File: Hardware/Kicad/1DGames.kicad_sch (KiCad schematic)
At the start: 0 parts

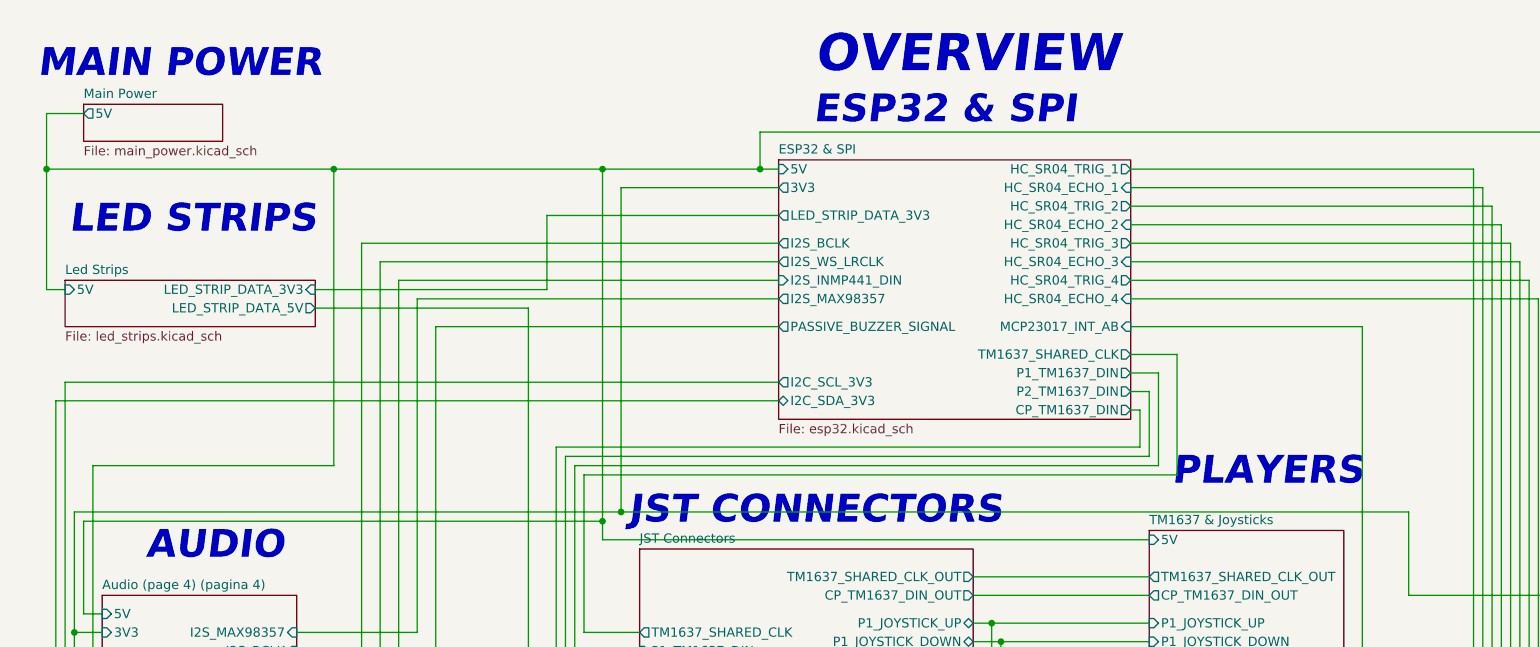
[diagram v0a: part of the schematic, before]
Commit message: New Fraxis PCB layout
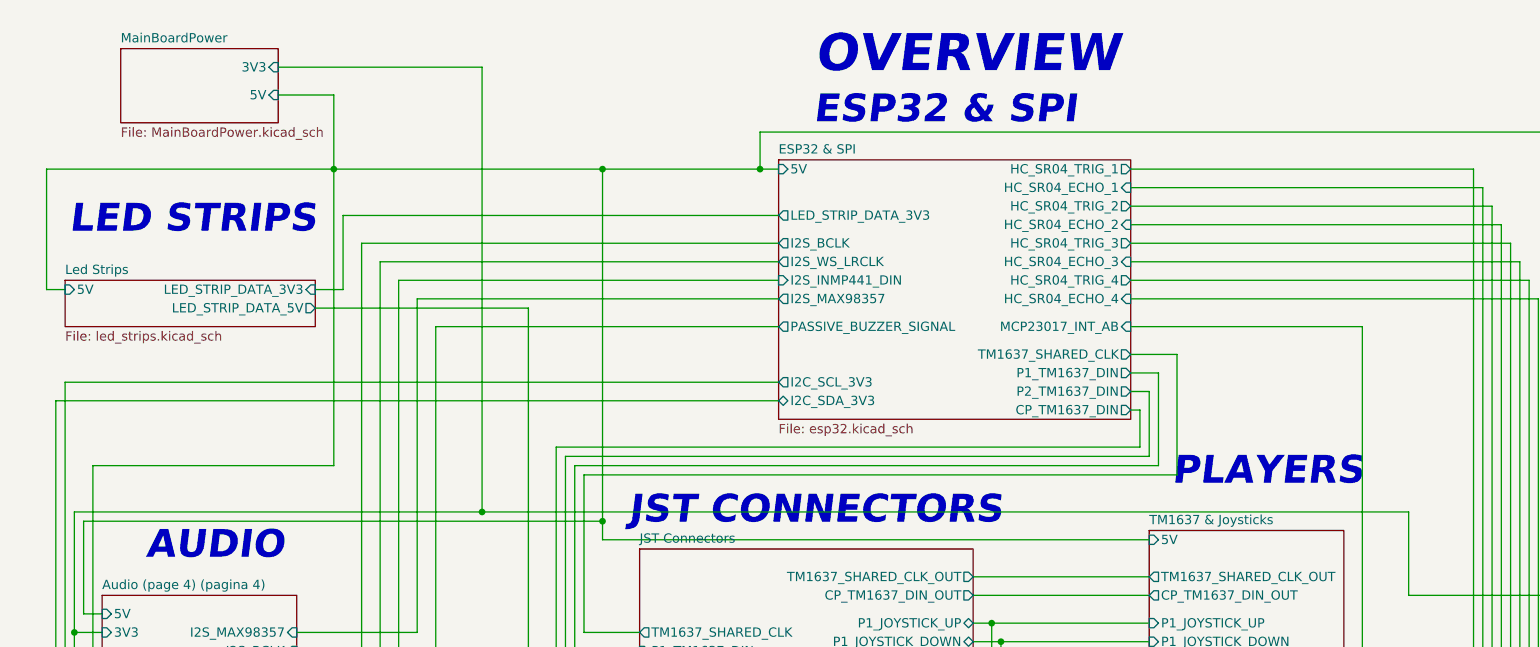
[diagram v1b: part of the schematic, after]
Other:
- removed sheet Main Power
- added sheet MainBoardPower (MainBoardPower.kicad_sch)
- sheet ESP32 & SPI ports: added none; removed 3V3
- note removed: "MAIN POWER"
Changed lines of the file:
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@@
 		)
 	)
-	(text "MAIN POWER"
-		(exclude_from_sim no)
-		(at 34.798 20.828 0)
-		(effects
-			(font
-				(size 3.81 3.81)
-				(thickness 0.4013)
-				(bold yes)
-				(italic yes)
-			)
-			(justify bottom)
-		)
-	)
 	(text "ESP32 & SPI"
 		(exclude_from_sim no)
@@
 	)
 	(junction
-		(at 95.25 80.01)
-		(diameter 0)
-		(color 0 0 0 0)
-	)
-	(junction
 		(at 212.09 113.03)
 		(diameter 0)
@@
 	)
 	(junction
-		(at 16.51 33.02)
+		(at 76.2 80.01)
 		(diameter 0)
 		(color 0 0 0 0)
@@
 	(wire
 		(pts
-			(xy 16.51 33.02) (xy 16.51 25.4)
-		)
-		(stroke
-			(width 0)
-			(type default)
-		)
-	)
-	(wire
-		(pts
 			(xy 87.63 135.89) (xy 87.63 113.03)
 		)
@@
 	(wire
 		(pts
+			(xy 48.26 22.86) (xy 55.88 22.86)
+		)
+		(stroke
+			(width 0)
+			(type default)
+		)
+	)
+	(wire
+		(pts
 			(xy 156.21 119.38) (xy 167.64 119.38)
 		)
@@
 	(wire
 		(pts
-			(xy 116.84 39.37) (xy 85.09 39.37)
+			(xy 57.15 39.37) (xy 116.84 39.37)
 		)
 		(stroke
@@
 	(wire
 		(pts
+			(xy 76.2 80.01) (xy 203.2 80.01)
+		)
+		(stroke
+			(width 0)
+			(type default)
+		)
+	)
+	(wire
+		(pts
 			(xy 143.51 157.48) (xy 213.36 157.48)
 		)
@@
 	(wire
 		(pts
-			(xy 16.51 25.4) (xy 21.59 25.4)
+			(xy 90.17 195.58) (xy 90.17 144.78)
 		)
 		(stroke
@@
 	(wire
 		(pts
-			(xy 90.17 195.58) (xy 90.17 144.78)
+			(xy 165.1 33.02) (xy 212.09 33.02)
 		)
 		(stroke
@@
 	(wire
 		(pts
-			(xy 165.1 33.02) (xy 212.09 33.02)
+			(xy 171.45 74.93) (xy 171.45 58.42)
 		)
 		(stroke
@@
 	(wire
 		(pts
-			(xy 171.45 74.93) (xy 171.45 58.42)
+			(xy 64.77 195.58) (xy 90.17 195.58)
 		)
 		(stroke
@@
 	(wire
 		(pts
-			(xy 64.77 195.58) (xy 90.17 195.58)
+			(xy 48.26 19.05) (xy 76.2 19.05)
 		)
 		(stroke
@@
 	(wire
 		(pts
-			(xy 20.32 80.01) (xy 95.25 80.01)
-		)
-		(stroke
-			(width 0)
-			(type default)
-		)
-	)
-	(wire
-		(pts
 			(xy 215.9 101.6) (xy 226.06 101.6)
 		)
@@
 	(wire
 		(pts
-			(xy 95.25 35.56) (xy 95.25 80.01)
-		)
-		(stroke
-			(width 0)
-			(type default)
-		)
-	)
-	(wire
-		(pts
 			(xy 143.51 142.24) (xy 165.1 142.24)
 		)
@@
 	(wire
 		(pts
-			(xy 95.25 80.01) (xy 203.2 80.01)
+			(xy 20.32 80.01) (xy 76.2 80.01)
 		)
 		(stroke
@@
 	(wire
 		(pts
-			(xy 95.25 35.56) (xy 116.84 35.56)
-		)
-		(stroke
-			(width 0)
-			(type default)
-		)
-	)
-	(wire
-		(pts
 			(xy 63.5 193.04) (xy 66.04 193.04)
 		)
@@
 	(wire
 		(pts
+			(xy 76.2 80.01) (xy 76.2 19.05)
+		)
+		(stroke
+			(width 0)
+			(type default)
+		)
+	)
+	(wire
+		(pts
 			(xy 24.13 157.48) (xy 20.32 157.48)
 		)
@@
 	(wire
 		(pts
+			(xy 55.88 33.02) (xy 55.88 22.86)
+		)
+		(stroke
+			(width 0)
+			(type default)
+		)
+	)
+	(wire
+		(pts
 			(xy 68.58 201.93) (xy 160.02 201.93)
 		)
@@
 	(wire
 		(pts
-			(xy 85.09 39.37) (xy 85.09 49.53)
-		)
-		(stroke
-			(width 0)
-			(type default)
-		)
-	)
-	(wire
-		(pts
 			(xy 92.71 33.02) (xy 114.3 33.02)
 		)
@@
 	(wire
 		(pts
-			(xy 53.34 49.53) (xy 85.09 49.53)
+			(xy 53.34 49.53) (xy 57.15 49.53)
 		)
 		(stroke
@@
 	(wire
 		(pts
+			(xy 57.15 49.53) (xy 57.15 39.37)
+		)
+		(stroke
+			(width 0)
+			(type default)
+		)
+	)
+	(wire
+		(pts
 			(xy 17.78 64.77) (xy 116.84 64.77)
 		)
@@
 	)
 	(sheet
+		(at 26.67 16.51)
+		(size 21.59 10.16)
+		(exclude_from_sim no)
+		(in_bom yes)
+		(on_board yes)
+		(dnp no)
+		(fields_autoplaced yes)
+		(stroke
+			(width 0.1524)
+			(type solid)
+		)
+		(fill
+			(color 0 0 0 0)
+		)
+		(property "Sheetname" "MainBoardPower"
+			(at 26.67 15.7984 0)
+			(show_name no)
+			(do_not_autoplace no)
+			(effects
+				(font
+					(size 1.27 1.27)
+				)
+				(justify left bottom)
+			)
+		)
+		(property "Sheetfile" "MainBoardPower.kicad_sch"
+			(at 26.67 27.2546 0)
+			(show_name no)
+			(do_not_autoplace no)
+			(effects
+				(font
+					(size 1.27 1.27)
+				)
+				(justify left top)
+			)
+		)
+		(pin "3V3" input
+			(at 48.26 19.05 0)
+			(effects
+				(font
+					(size 1.27 1.27)
+				)
+				(justify right)
+			)
+		)
+		(pin "5V" input
+			(at 48.26 22.86 0)
+			(effects
+				(font
+					(size 1.27 1.27)
+				)
+				(justify right)
+			)
+		)
+		(instances
+			(project "1DGames"
+				(path "/b1c649b1-f44d-46c7-9dea-818e75a1b87e"
+					(page "2")
+				)
+			)
+		)
+	)
+	(sheet
 		(at 167.64 82.55)
 		(size 26.67 66.04)
@@
 			)
 		)
-		(pin "3V3" output
-			(at 116.84 35.56 180)
-			(effects
-				(font
-					(size 1.27 1.27)
-				)
-				(justify left)
-			)
-		)
 		(pin "CP_TM1637_DIN" output
 			(at 165.1 66.04 0)
@@
 				)
 			)
-		)
-	)
-	(sheet
-		(at 21.59 24.13)
-		(size 19.05 5.08)
-		(exclude_from_sim no)
-		(in_bom yes)
-		(on_board yes)
-		(dnp no)
-		(fields_autoplaced yes)
-		(stroke
-			(width 0.1524)
-			(type solid)
-		)
-		(fill
-			(color 0 0 0 0)
-		)
-		(property "Sheetname" "Main Power"
-			(at 21.59 23.4184 0)
-			(show_name no)
-			(do_not_autoplace no)
-			(effects
-				(font
-					(size 1.27 1.27)
-				)
-				(justify left bottom)
-			)
-		)
-		(property "Sheetfile" "main_power.kicad_sch"
-			(at 21.59 29.7946 0)
-			(show_name no)
-			(do_not_autoplace no)
-			(effects
-				(font
-					(size 1.27 1.27)
-				)
-				(justify left top)
-			)
-		)
-		(pin "5V" output
-			(at 21.59 25.4 180)
-			(effects
-				(font
-					(size 1.27 1.27)
-				)
-				(justify left)
-			)
-		)
-		(instances
-			(project "1DGames"
-				(path "/b1c649b1-f44d-46c7-9dea-818e75a1b87e"
-					(page "2")
-				)
-			)
